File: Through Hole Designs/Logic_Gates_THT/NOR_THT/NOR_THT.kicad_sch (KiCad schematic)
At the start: 89 parts, among them J1 AudioJack1_Switch, J10 Conn_01x08, J11 Conn_01x08, J12 Conn_01x08, J13 Conn_02x08_Odd_Even, J14 Conn_01x12, J15 Conn_01x12, J16 AudioJack1_Switch, J17 AudioJack1_Switch, J18 AudioJack1_Switch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

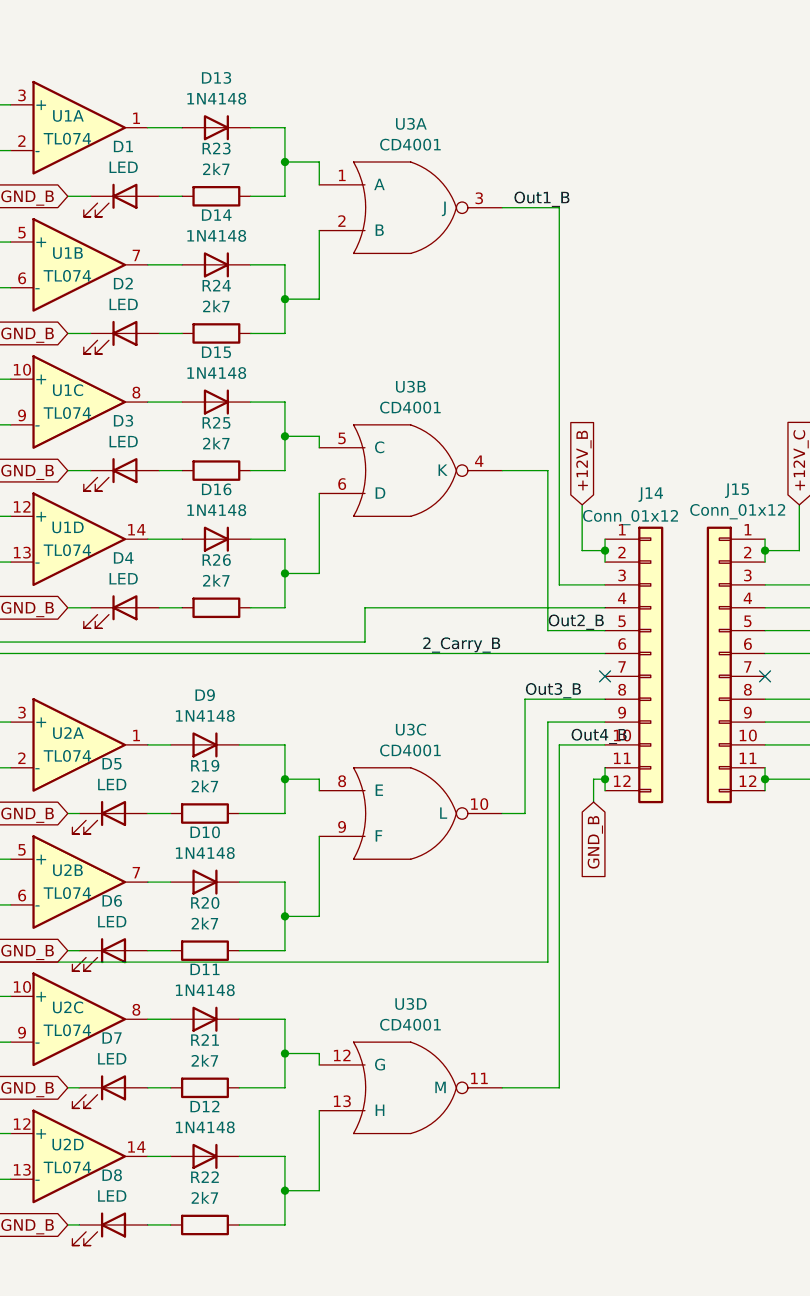
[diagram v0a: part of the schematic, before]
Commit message: KiCad 9.0 Update
Installed KiCad 9.0 and updated all the files to latest version before continuing work on the designs.
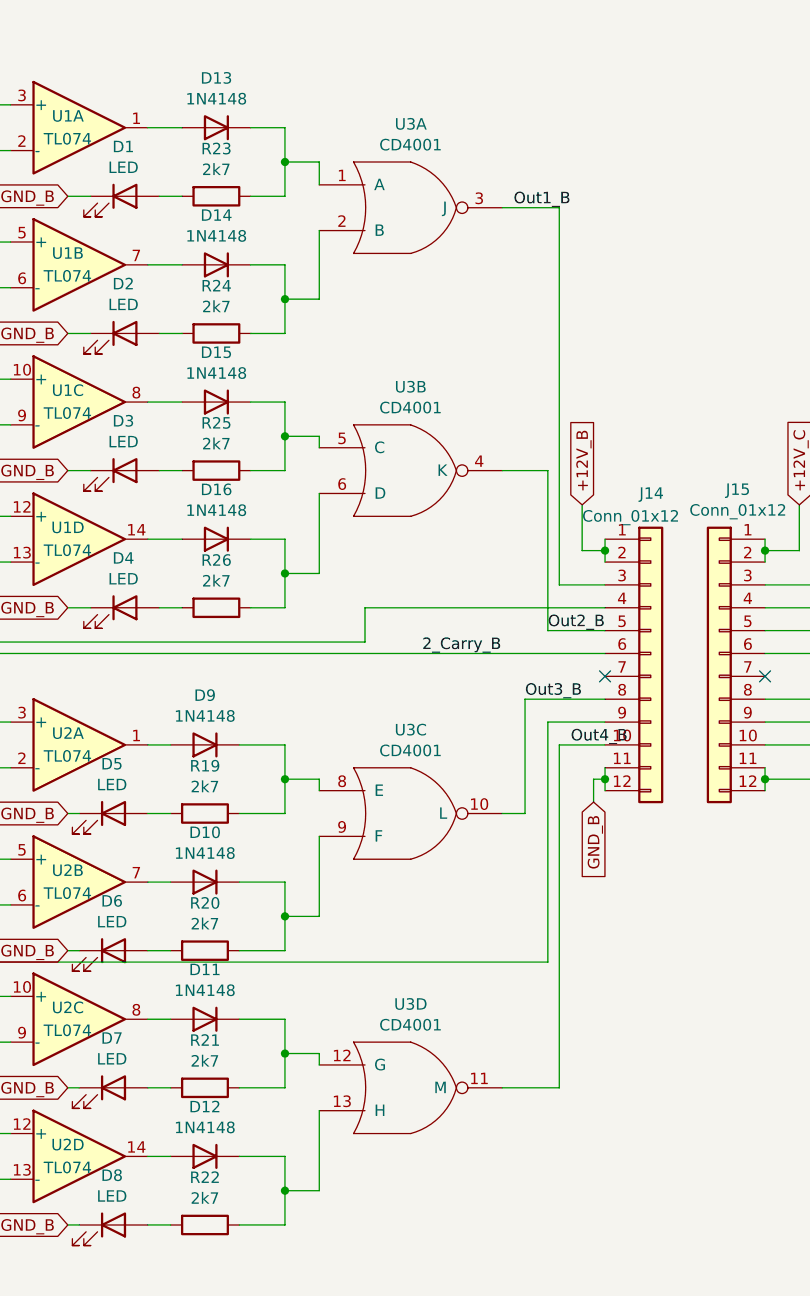
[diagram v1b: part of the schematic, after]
